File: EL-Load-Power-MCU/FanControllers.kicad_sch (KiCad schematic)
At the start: 28 parts, among them J5 PN sensor, J6 PN sensor, M1 Fan_4pin, M2 Fan_4pin, M3 Fan_4pin, U1 MAX31760, U3 MAX31760

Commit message: Fixed Panel 1r1 and Power-MCU 2r2 versions
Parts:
- C10, C11, C12, C15, C8: Part_Name (none) -> C_100.0nF_50V_0805_10%
- C14: MPN (none) -> EEE-FK1V470P; Part_Name (none) -> C_47u_35V_Elec_6.3_20%
- D10, D11, D5: Part_Name (none) -> D_SS14
- J5, J6: Consumable (none) -> 1; Part_Name (none) -> H_Male_1x40_vertical_THT
- JP2, JP3: now left out of the parts list
- R1, R2, R6, R7: Part_Name (none) -> R_4.7kΩ_0805_1%
- R10, R3, R8: Part_Name (none) -> R_10.0Ω_0805_1%
- R11, R5, R9: Part_Name (none) -> R_1.0kΩ_0805_1%
- U1, U3: Part_Name (none) -> U_MAX31760AEE+T

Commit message: BOM fixes/updates.
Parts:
- M1, M2, M3: Part_Name (none) -> H_Molex_47053-1000_THT_PC_Fan
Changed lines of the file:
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@@
       (effects (font (size 1.27 1.27)))
     )
-    (property "Part_Name" "" (at 211.455 57.785 0)
+    (property "Part_Name" "H_Molex_47053-1000_THT_PC_Fan" (at 211.455 57.785 0)
       (effects (font (size 1.27 1.27)) hide)
     )
@@
       (effects (font (size 1.27 1.27)))
     )
-    (property "Part_Name" "" (at 211.455 142.875 0)
+    (property "Part_Name" "H_Molex_47053-1000_THT_PC_Fan" (at 211.455 142.875 0)
       (effects (font (size 1.27 1.27)) hide)
     )
@@
       (effects (font (size 1.27 1.27)))
     )
-    (property "Part_Name" "" (at 211.455 120.015 0)
-      (effects (font (size 1.27 1.27)) hide)
-    )
+    (property "Part_Name" "H_Molex_47053-1000_THT_PC_Fan" (at 211.455 120.015 0)
+      (effects (font (size 1.27 1.27)) hide)
+    )

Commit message: Fixes to Power-MCU board.
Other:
- title: EL-Load-PowerTest2 -> EL-Load-Power-MCU
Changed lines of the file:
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@@
   (paper "A4")
   (title_block
-    (title "EL-Load-PowerTest2")
-    (date "2023-11-28")
+    (title "EL-Load-Power-MCU")
+    (date "2024-02-04")
     (rev "${VERSION}r${PCBVERSION}")
   )

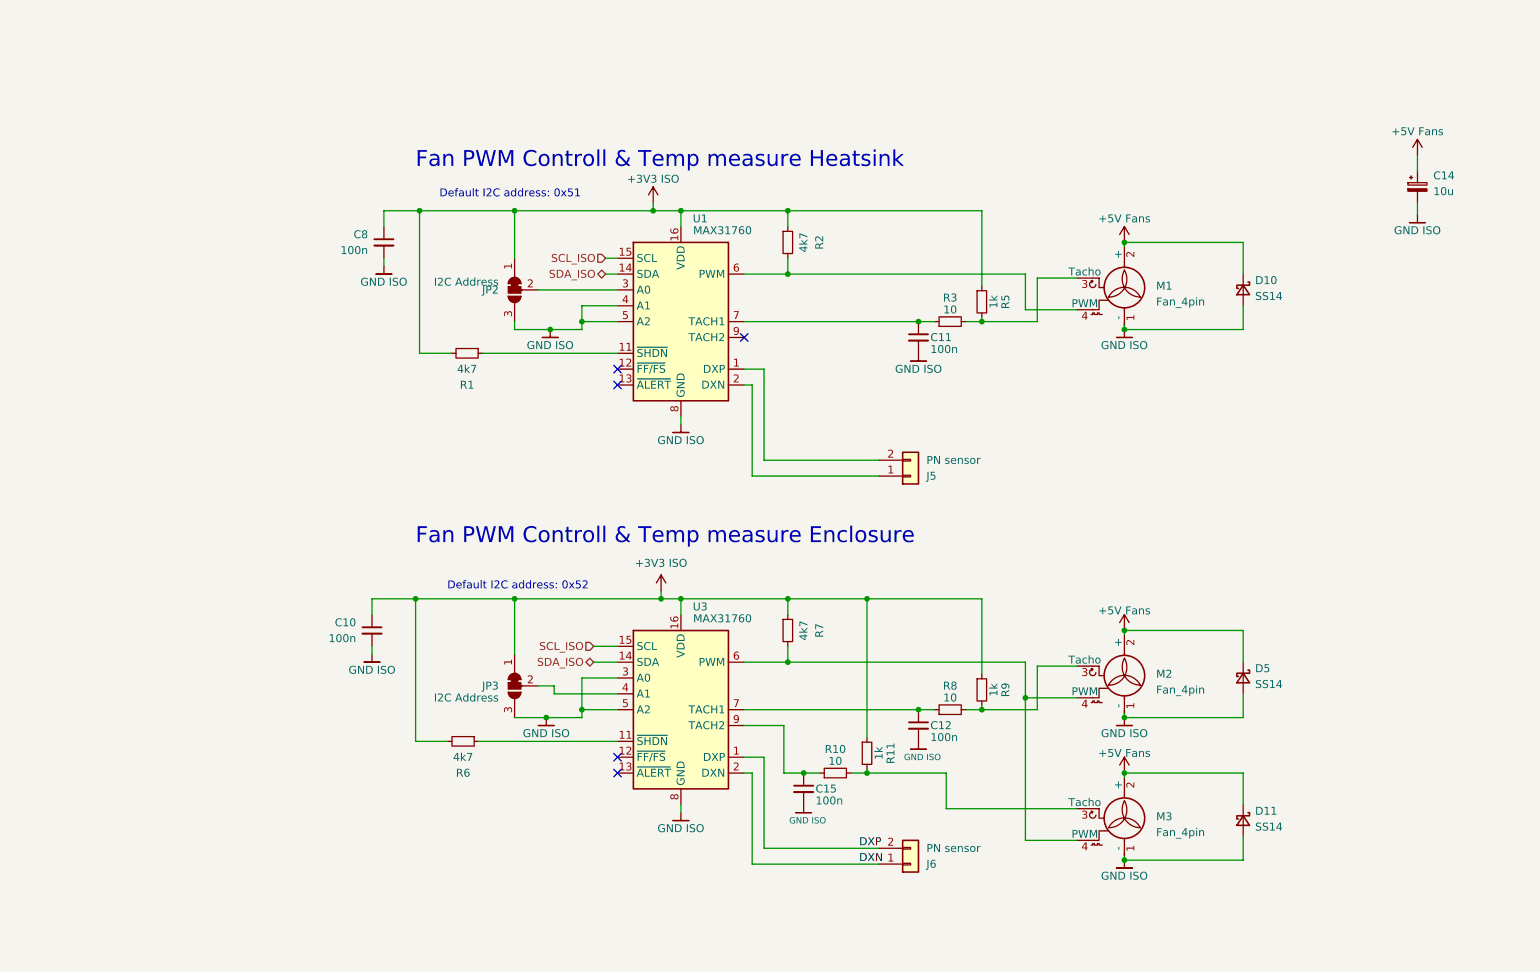
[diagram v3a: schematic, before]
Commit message: Added +15VU led, fixed JP1
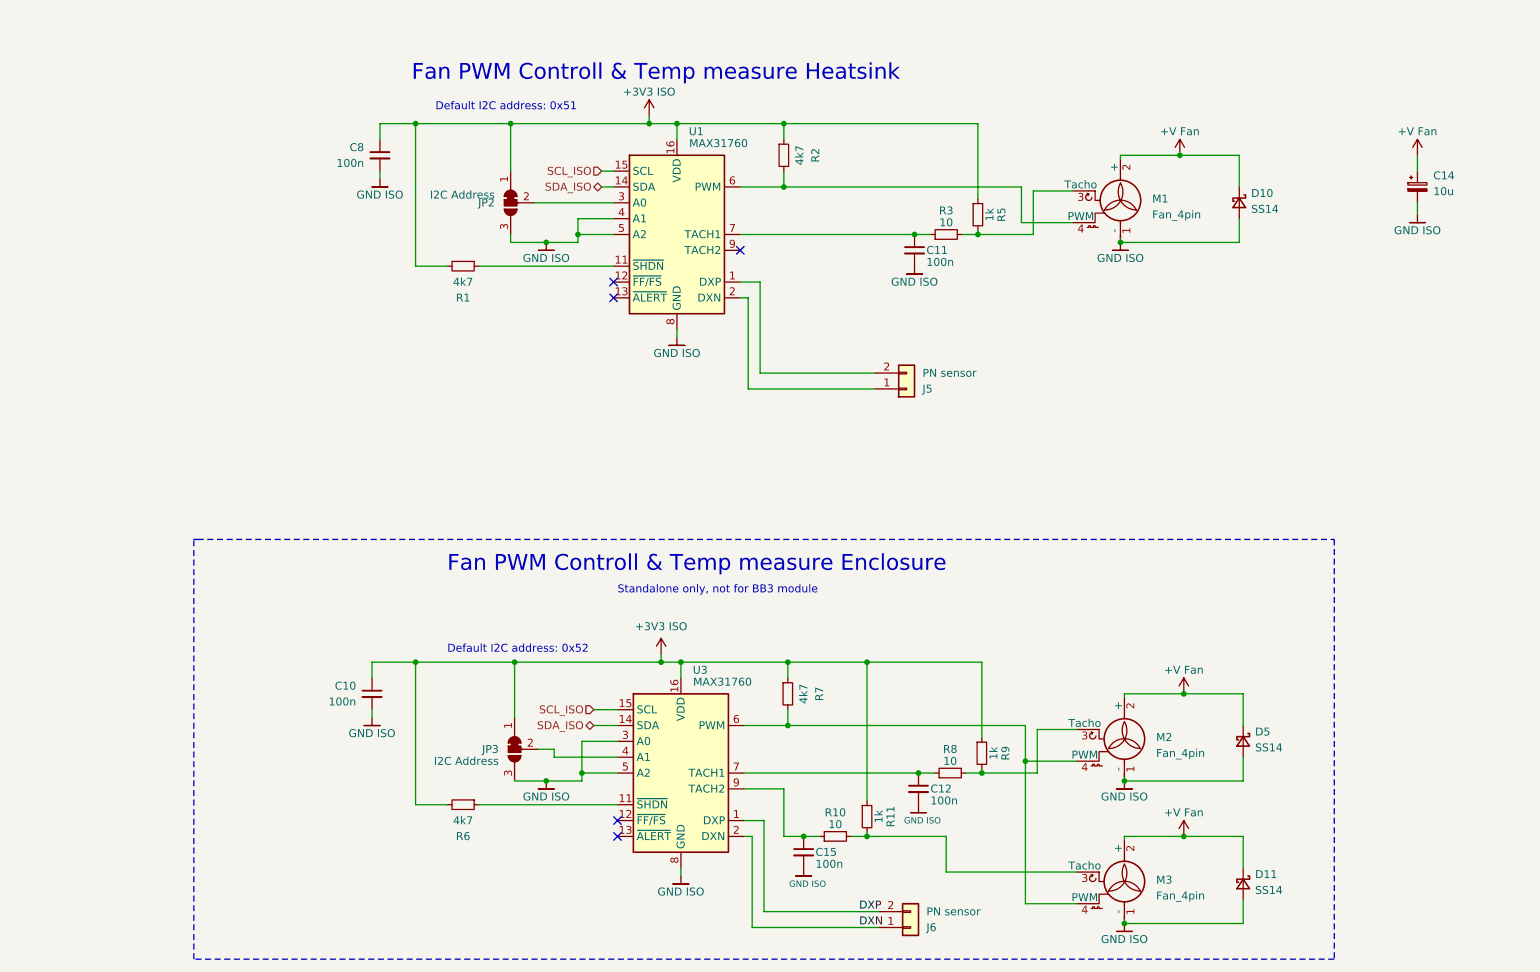
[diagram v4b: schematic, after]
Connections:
- net +5V_FANS renamed +V_FANS
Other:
- note added: "Standalone only, not for BB3 module"
- moved on the sheet: C10, C11, C12, C15, C8, D10, D11, D5, J5, J6, JP2, JP3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

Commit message: EL-Load-Power-MCU PCB v4r4 release.
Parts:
- removed C14: 10u, Capacitor_SMD:CP_Elec_6.3x5.8, symbol Device:C_Polarized_Small
- removed C15: 100n, Capacitor_SMD:C_0805_2012Metric, symbol Device:C_Small
- removed D11: SS14, Diode_SMD:D_SMA, symbol Device:D_Schottky_Small
- removed J6: PN sensor, Connector_PinHeader_2.54mm:PinHeader_1x02_P2.54mm_Vertical, symbol Connector_Generic:Conn_01x02
- removed JP3: I2C Address, Jumper:SolderJumper-3_P1.3mm_Bridged2Bar12_RoundedPad1.0x1.5mm, symbol Jumper:SolderJumper_3_Bridged12
- removed M3: Fan_4pin, Connector:FanPinHeader_1x04_P2.54mm_Vertical, symbol Motor:Fan_4pin
- removed U3: MAX31760, Package_SO:QSOP-16_3.9x4.9mm_P0.635mm, symbol EL-Load:MAX31760
- added C14: 1u, Capacitor_SMD:C_0805_2012Metric, symbol Device:C_Small
- added C15: 10u, Capacitor_SMD:CP_Elec_5x5.8, symbol Device:C_Polarized_Small
- added JP5: LDO En, Connector_PinHeader_2.54mm:PinHeader_1x02_P2.54mm_Vertical, symbol Jumper:Jumper_2_Bridged
- added JP8: Fan Volt/PWM, Connector_PinHeader_2.54mm:PinHeader_1x03_P2.54mm_Vertical, symbol Jumper:Jumper_3_Open
- added R28: 10k, Resistor_SMD:R_0805_2012Metric, symbol Device:R_Small
- added U3: BD00FC0WFP-E2, Package_TO_SOT_SMD:TO-252-5_TabPin6, symbol EL-Load:BD00FC0W
- C10, C11, C8: Part_Name C_100.0nF_50V_0805_10% -> C_100.0nF_50V_0805_10%_X7R
- C12: value 100n -> 2.2u; Part_Name C_100.0nF_50V_0805_10% -> C_2.2uF_25V_X7R_10%_0805
- R1, R2, R3, R5: footprint Resistor_SMD:R_0805_2012Metric_Pad1.20x1.40mm_HandSolder -> Resistor_SMD:R_0805_2012Metric
- R10: value 10 -> 3k3; footprint Resistor_SMD:R_0805_2012Metric_Pad1.20x1.40mm_HandSolder -> Resistor_SMD:R_0805_2012Metric; Part_Name R_10.0Ω_0805_1% -> R_3.3kΩ_0805_1%
- R11: value 1k -> 3k3; footprint Resistor_SMD:R_0805_2012Metric_Pad1.20x1.40mm_HandSolder -> Resistor_SMD:R_0805_2012Metric; Part_Name R_1.0kΩ_0805_1% -> R_3.3kΩ_0805_1%
- R6: value 4k7 -> 10; footprint Resistor_SMD:R_0805_2012Metric_Pad1.20x1.40mm_HandSolder -> Resistor_SMD:R_0805_2012Metric; Part_Name R_4.7kΩ_0805_1% -> R_10.0Ω_0805_1%
- R7: value 4k7 -> 1k; footprint Resistor_SMD:R_0805_2012Metric_Pad1.20x1.40mm_HandSolder -> Resistor_SMD:R_0805_2012Metric; Part_Name R_4.7kΩ_0805_1% -> R_1.0kΩ_0805_1%
- R8: value 10 -> 1k; footprint Resistor_SMD:R_0805_2012Metric_Pad1.20x1.40mm_HandSolder -> Resistor_SMD:R_0805_2012Metric; Part_Name R_10.0Ω_0805_1% -> R_1.0kΩ_0805_1%
- R9: value 1k -> 39k; footprint Resistor_SMD:R_0805_2012Metric_Pad1.20x1.40mm_HandSolder -> Resistor_SMD:R_0805_2012Metric; Part_Name R_1.0kΩ_0805_1% -> R_39.0kΩ_0805_1%
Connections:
- net +3V3_ISO: no longer C10.1, R11.1, R6.2, R9.1
- net +V_FANS: now also C12.1, JP5.2 (B), JP8.3 (B), U3.2 (Vcc); no longer D10.1 (K), D5.1 (K), M1.2 (+), M2.2 (+)
- net GND_ISO: now also R10.2, C14.2, C15.2, R28.1, U3.6 (GND)
- net Fan1PWM: now reaches R8.1
- net Fan1PWM: now also M1.4 (PWM), M2.4 (PWM), R2.2, U1.6 (PWM); no longer C12.1
- net Fan2Tacho: now reaches R7.2
- net Fan2Tacho: now also M2.3 (Tacho), R6.2; no longer M2.4 (PWM)
- net at R6.1: now also C10.1, U1.9 (TACH2)
- net at R11.2: now also R8.2, C14.1; no longer R10.2
- net at R10.1: now also R11.1, R9.2, U3.5 (FB)
- net Fan1Tacho: now reaches M1.3 (Tacho), R3.2, R5.2
- new net: JP5.1 (A), R28.2, U3.1 (EN)
- new net: JP8.1 (A), R9.1, U3.4 (VOUT)
- new net Fan1PWR: C15.1, D10.1 (K), D5.1 (K), JP8.2 (C), M1.2 (+), M2.2 (+)
- no-connect marks 5 -> 2
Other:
- note removed: "Default I2C address: 0x52"
- note removed: "Fan PWM Controll & Temp measure Enclosure"
- note removed: "Standalone only, not for BB3 module"
- moved on the sheet: C11, C8, D10, J5, JP2, M1, R1, R2, R3, R5, U1

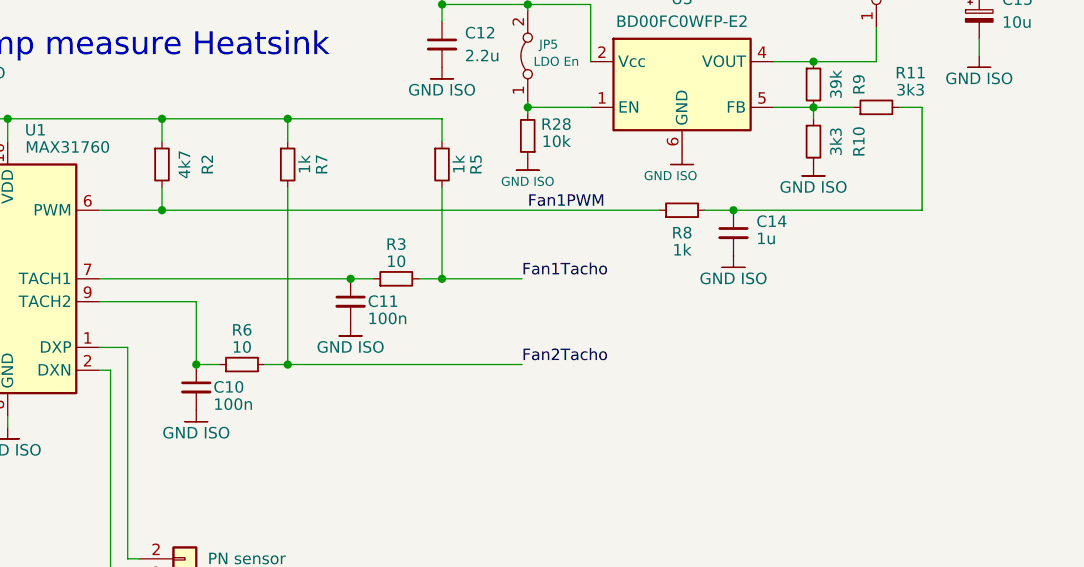
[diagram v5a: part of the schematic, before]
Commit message: Fixed fan driver with jumper. Initial v5 version (still KiCad7)
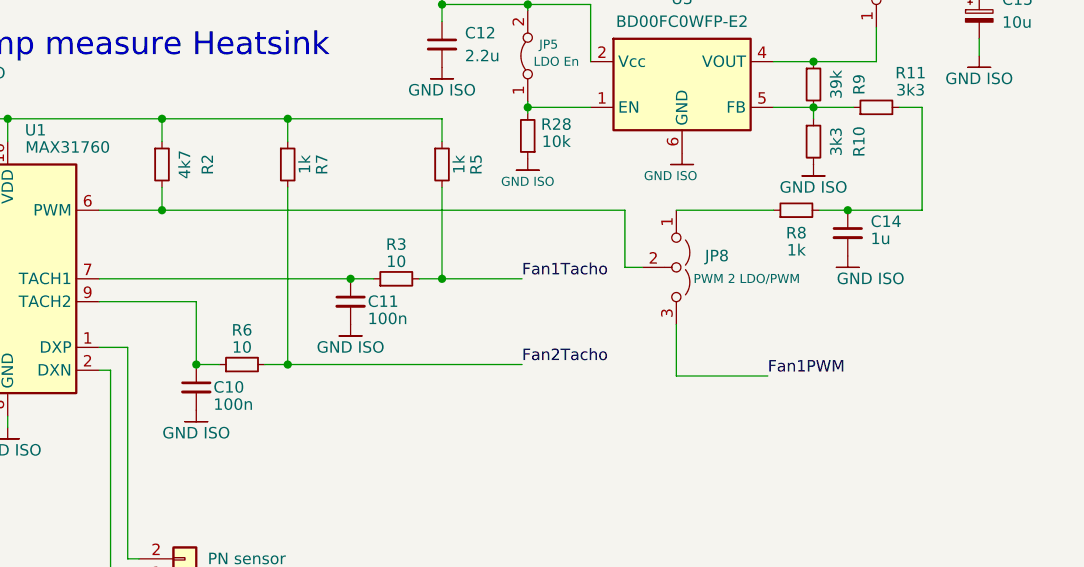
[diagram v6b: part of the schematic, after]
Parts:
- added JP8: PWM 2 LDO/PWM, Connector_PinHeader_2.54mm:PinHeader_1x03_P2.54mm_Vertical, symbol Jumper:Jumper_3_Open
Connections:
- net Fan1PWM: now also JP8.3 (B); no longer R2.2, R8.1, U1.6 (PWM)
- new net: JP8.1 (A), R8.1
- new net: JP8.2 (C), R2.2, U1.6 (PWM)
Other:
- moved on the sheet: C14, R8
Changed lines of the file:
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@@
   (junction (at 67.945 59.69) (diameter 0) (color 0 0 0 0)
   )
-  (junction (at 169.545 50.8) (diameter 0) (color 0 0 0 0)
+  (junction (at 182.245 50.8) (diameter 0) (color 0 0 0 0)
   )
   (junction (at 253.365 69.85) (diameter 0) (color 0 0 0 0)
@@
   (junction (at 137.16 58.42) (diameter 0) (color 0 0 0 0)
   )
+  (junction (at 146.685 27.94) (diameter 0) (color 0 0 0 0)
+  )
   (junction (at 106.045 50.8) (diameter 0) (color 0 0 0 0)
-  )
-  (junction (at 146.685 27.94) (diameter 0) (color 0 0 0 0)
   )
   (no_connect (at 78.74 68.58))
@@
     (stroke (width 0) (type default))
   )
+  (wire (pts (xy 163.195 69.215) (xy 173.355 69.215))
+    (stroke (width 0) (type default))
+  )
   (wire (pts (xy 253.365 69.85) (xy 268.605 69.85))
     (stroke (width 0) (type default))
@@
     (stroke (width 0) (type default))
   )
+  (wire (pts (xy 163.195 63.5) (xy 163.195 69.215))
+    (stroke (width 0) (type default))
+  )
   (wire (pts (xy 41.275 40.64) (xy 46.99 40.64))
     (stroke (width 0) (type default))
@@
     (stroke (width 0) (type default))
   )
+  (wire (pts (xy 157.48 57.15) (xy 159.385 57.15))
+    (stroke (width 0) (type default))
+  )
   (wire (pts (xy 62.23 40.64) (xy 84.455 40.64))
     (stroke (width 0) (type default))
@@
     (stroke (width 0) (type default))
   )
+  (wire (pts (xy 163.195 50.8) (xy 173.99 50.8))
+    (stroke (width 0) (type default))
+  )
   (wire (pts (xy 73.025 55.88) (xy 73.025 58.42))
     (stroke (width 0) (type default))
@@
     (stroke (width 0) (type default))
   )
-  (wire (pts (xy 106.045 50.8) (xy 161.29 50.8))
+  (wire (pts (xy 106.045 50.8) (xy 157.48 50.8))
     (stroke (width 0) (type default))
   )
@@
     (stroke (width 0) (type default))
   )
-  (wire (pts (xy 190.5 50.8) (xy 169.545 50.8))
+  (wire (pts (xy 190.5 50.8) (xy 182.245 50.8))
     (stroke (width 0) (type default))
   )
@@
     (stroke (width 0) (type default))
   )
-  (wire (pts (xy 166.37 50.8) (xy 169.545 50.8))
+  (wire (pts (xy 157.48 50.8) (xy 157.48 57.15))
+    (stroke (width 0) (type default))
+  )
+  (wire (pts (xy 179.07 50.8) (xy 182.245 50.8))
     (stroke (width 0) (type default))
   )
@@
     (effects (font (size 1.27 1.27)) (justify left bottom))
   )
-  (label "Fan1PWM" (at 146.685 50.8 0) (fields_autoplaced)
+  (label "Fan1PWM" (at 173.355 69.215 0) (fields_autoplaced)
     (effects (font (size 1.27 1.27)) (justify left bottom))
   )
@@
     )
   )
-  (symbol (lib_id "EL-Load-Power:GND ISO") (at 169.545 55.88 0) (unit 1)
-    (in_bom yes) (on_board yes) (dnp no)
-    (property "Reference" "#PWR?" (at 169.545 62.23 0)
-      (effects (font (size 1.27 1.27)) hide)
-    )
-    (property "Value" "GND ISO" (at 169.545 58.42 0)
-      (effects (font (size 1.27 1.27)))
-    )
-    (property "Footprint" "" (at 169.545 55.88 0)
-      (effects (font (size 1.27 1.27)) hide)
-    )
-    (property "Datasheet" "" (at 169.545 55.88 0)
+  (symbol (lib_id "EL-Load-Power:GND ISO") (at 182.245 55.88 0) (unit 1)
+    (in_bom yes) (on_board yes) (dnp no)
+    (property "Reference" "#PWR?" (at 182.245 62.23 0)
+      (effects (font (size 1.27 1.27)) hide)
+    )
+    (property "Value" "GND ISO" (at 184.785 58.42 0)
+      (effects (font (size 1.27 1.27)))
+    )
+    (property "Footprint" "" (at 182.245 55.88 0)
+      (effects (font (size 1.27 1.27)) hide)
+    )
+    (property "Datasheet" "" (at 182.245 55.88 0)
       (effects (font (size 1.27 1.27)) hide)
     )
@@
     )
   )
-  (symbol (lib_id "Device:R_Small") (at 163.83 50.8 90) (unit 1)
-    (in_bom yes) (on_board yes) (dnp no)
-    (property "Reference" "R8" (at 163.83 53.34 90)
-      (effects (font (size 1.27 1.27)))
-    )
-    (property "Value" "1k" (at 163.83 55.245 90)
-      (effects (font (size 1.27 1.27)))
-    )
-    (property "Footprint" "Resistor_SMD:R_0805_2012Metric" (at 163.83 50.8 0)
-      (effects (font (size 1.27 1.27)) hide)
-    )
-    (property "Datasheet" "~" (at 163.83 50.8 0)
-      (effects (font (size 1.27 1.27)) hide)
-    )
-    (property "Part_Name" "R_1.0kΩ_0805_1%" (at 163.83 50.8 0)
+  (symbol (lib_id "Device:R_Small") (at 176.53 50.8 90) (unit 1)
+    (in_bom yes) (on_board yes) (dnp no)
+    (property "Reference" "R8" (at 176.53 53.34 90)
+      (effects (font (size 1.27 1.27)))
+    )
+    (property "Value" "1k" (at 176.53 55.245 90)
+      (effects (font (size 1.27 1.27)))
+    )
+    (property "Footprint" "Resistor_SMD:R_0805_2012Metric" (at 176.53 50.8 0)
+      (effects (font (size 1.27 1.27)) hide)
+    )
+    (property "Datasheet" "~" (at 176.53 50.8 0)
+      (effects (font (size 1.27 1.27)) hide)
+    )
+    (property "Part_Name" "R_1.0kΩ_0805_1%" (at 176.53 50.8 0)
       (effects (font (size 1.27 1.27)) hide)
     )
@@
     )
   )
+  (symbol (lib_id "Jumper:Jumper_3_Open") (at 163.195 57.15 270) (unit 1)
+    (in_bom yes) (on_board yes) (dnp no)
+    (property "Reference" "JP8" (at 166.37 55.88 90)
+      (effects (font (size 1.27 1.27)) (justify left))
+    )
+    (property "Value" "PWM 2 LDO/PWM" (at 165.1 58.42 90)
+      (effects (font (size 1 1)) (justify left))
+    )
+    (property "Footprint" "Connector_PinHeader_2.54mm:PinHeader_1x03_P2.54mm_Vertical" (at 163.195 57.15 0)
+      (effects (font (size 1.27 1.27)) hide)
+    )
+    (property "Datasheet" "~" (at 163.195 57.15 0)
+      (effects (font (size 1.27 1.27)) hide)
+    )
+    (property "MPN" "" (at 163.195 57.15 0)
+      (effects (font (size 1.27 1.27)))
+    )
+    (property "Consumable" "1" (at 163.195 57.15 0)
+      (effects (font (size 1.27 1.27)) hide)
+    )
+    (property "Part_Name" "H_Male_1x40_vertical_THT " (at 163.195 57.15 0)
+      (effects (font (size 1.27 1.27)) hide)
+    )
+    (pin "1")
+    (pin "2")
+    (pin "3")
+    (instances
+      (project "EL-Load-Power-MCU"
+        (path "/49e2a88f-ac55-47e0-a814-2d050901620c"
+          (reference "JP8") (unit 1)
+        )
+        (path "/49e2a88f-ac55-47e0-a814-2d050901620c/2e7c8fcf-b465-4e9c-8894-099a4c590949"
+          (reference "JP13") (unit 1)
+        )
+      )
+    )
+  )
   (symbol (lib_id "EL-Load-Power:GND ISO") (at 137.16 34.925 0) (unit 1)
     (in_bom yes) (on_board yes) (dnp no)
@@
     )
   )
-  (symbol (lib_id "Device:C_Small") (at 169.545 53.34 0) (unit 1)
-    (in_bom yes) (on_board yes) (dnp no)
-    (property "Reference" "C14" (at 172.085 52.07 0)
-      (effects (font (size 1.27 1.27)) (justify left))
-    )
-    (property "Value" "1u" (at 172.085 53.975 0)
-      (effects (font (size 1.27 1.27)) (justify left))
-    )
-    (property "Footprint" "Capacitor_SMD:C_0805_2012Metric" (at 169.545 53.34 0)
-      (effects (font (size 1.27 1.27)) hide)
-    )
-    (property "Datasheet" "~" (at 169.545 53.34 0)
-      (effects (font (size 1.27 1.27)) hide)
-    )
-    (property "Part_Name" "C_1.0uF_0805_20%" (at 169.545 53.34 0)
-      (effects (font (size 1.27 1.27)) hide)
-    )
+  (symbol (lib_id "Device:C_Small") (at 182.245 53.34 0) (unit 1)
+    (in_bom yes) (on_board yes) (dnp no)
+    (property "Reference" "C14" (at 184.785 52.07 0)
+      (effects (font (size 1.27 1.27)) (justify left))
+    )
+    (property "Value" "1u" (at 184.785 53.975 0)
+      (effects (font (size 1.27 1.27)) (justify left))
+    )
+    (property "Footprint" "Capacitor_SMD:C_0805_2012Metric" (at 182.245 53.34 0)
+      (effects (font (size 1.27 1.27)) hide)
+    )
+    (property "Datasheet" "~" (at 182.245 53.34 0)
+      (effects (font (size 1.27 1.27)) hide)
+    )
+    (property "Part_Name" "C_1.0uF_0805_20%" (at 182.245 53.34 0)
+      (effects (font (size 1.27 1.27)) hide)
+    )
